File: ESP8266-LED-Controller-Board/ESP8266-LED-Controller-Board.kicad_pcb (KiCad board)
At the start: 2 copper layers, 70 x 38 mm, 52 parts, among them J1 Barrel_Jack_Switch, J2 USB_C_Receptacle_USB2.0, J3 Conn_01x04_Male, J4 Conn_01x05_Male, J5 Screw_Terminal_01x04, J6 Screw_Terminal_01x02, Q1 NTD5867NLT4G, Q2 NTD5867NLT4G, Q3 NTD5867NLT4G, Q4 NTD5867NLT4G, Q5 NTD5867NLT4G, SW1 SW_Push, SW2 SW_Push, U1 TPS563200, U2 ACS70331EESATR-005U3, U3 ESP-12F, U4 74LVC2G17DBVR

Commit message: Updated readme and part number.
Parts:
- U4: value 74LVC2G17DBVR -> SN74LVC2G17DCKR
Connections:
- J2 pad A6: (no net) -> Net-(J2-PadA6)
- J2 pad A7: (no net) -> Net-(J2-PadA7)
- J2 pad A8: (no net) -> Net-(J2-PadA8)
- J2 pad B6: (no net) -> Net-(J2-PadB6)
- J2 pad B7: (no net) -> Net-(J2-PadB7)
- J2 pad B8: (no net) -> Net-(J2-PadB8)
- U3 pad 10: (no net) -> Net-(U3-Pad10)
- U3 pad 13: (no net) -> Net-(U3-Pad13)
- U3 pad 14: (no net) -> Net-(U3-Pad14)
- U3 pad 9: (no net) -> Net-(U3-Pad9)
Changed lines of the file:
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@@
     (zones 0)
     (modules 52)
-    (nets 42)
+    (nets 52)
   )
   (page A4)
@@
   (net 40 "Net-(R7-Pad1)")
   (net 41 "Net-(R11-Pad2)")
+  (net 42 "Net-(J2-PadB6)")
+  (net 43 "Net-(J2-PadA8)")
+  (net 44 "Net-(J2-PadB8)")
+  (net 45 "Net-(J2-PadA7)")
+  (net 46 "Net-(J2-PadA6)")
+  (net 47 "Net-(J2-PadB7)")
+  (net 48 "Net-(U3-Pad14)")
+  (net 49 "Net-(U3-Pad13)")
+  (net 50 "Net-(U3-Pad10)")
+  (net 51 "Net-(U3-Pad9)")
   (net_class Default "This is the default net class."
     (clearance 0.2)
@@
     (add_net "Net-(C2-Pad2)")
     (add_net "Net-(J2-PadA5)")
+    (add_net "Net-(J2-PadA6)")
+    (add_net "Net-(J2-PadA7)")
+    (add_net "Net-(J2-PadA8)")
     (add_net "Net-(J2-PadB5)")
+    (add_net "Net-(J2-PadB6)")
+    (add_net "Net-(J2-PadB7)")
+    (add_net "Net-(J2-PadB8)")
     (add_net "Net-(Q1-Pad1)")
     (add_net "Net-(Q2-Pad1)")
@@
     (add_net "Net-(R5-Pad2)")
     (add_net "Net-(R7-Pad1)")
+    (add_net "Net-(U3-Pad10)")
+    (add_net "Net-(U3-Pad13)")
+    (add_net "Net-(U3-Pad14)")
+    (add_net "Net-(U3-Pad9)")
     (add_net VDD)
     (add_net VIN)
@@
     (pad 15 smd rect (at 7.6 10.5) (size 2.5 1) (layers F.Cu F.Paste F.Mask)
       (net 6 GND))
-    (pad 14 smd rect (at 5 12) (size 1 1.8) (layers F.Cu F.Paste F.Mask))
-    (pad 13 smd rect (at 3 12) (size 1 1.8) (layers F.Cu F.Paste F.Mask))
+    (pad 14 smd rect (at 5 12) (size 1 1.8) (layers F.Cu F.Paste F.Mask)
+      (net 48 "Net-(U3-Pad14)"))
+    (pad 13 smd rect (at 3 12) (size 1 1.8) (layers F.Cu F.Paste F.Mask)
+      (net 49 "Net-(U3-Pad13)"))
     (pad 12 smd rect (at 1 12) (size 1 1.8) (layers F.Cu F.Paste F.Mask)
       (net 28 /LED_G_CTRL))
     (pad 11 smd rect (at -1 12) (size 1 1.8) (layers F.Cu F.Paste F.Mask)
       (net 29 /LED_B_CTRL))
-    (pad 10 smd rect (at -3 12) (size 1 1.8) (layers F.Cu F.Paste F.Mask))
-    (pad 9 smd rect (at -5 12) (size 1 1.8) (layers F.Cu F.Paste F.Mask))
+    (pad 10 smd rect (at -3 12) (size 1 1.8) (layers F.Cu F.Paste F.Mask)
+      (net 50 "Net-(U3-Pad10)"))
+    (pad 9 smd rect (at -5 12) (size 1 1.8) (layers F.Cu F.Paste F.Mask)
+      (net 51 "Net-(U3-Pad9)"))
     (pad 8 smd rect (at -7.6 10.5) (size 2.5 1) (layers F.Cu F.Paste F.Mask)
       (net 7 +3V3))
@@
     (pad B5 smd rect (at 1.75 -2.51 90) (size 0.3 1.16) (layers F.Cu F.Paste F.Mask)
       (net 35 "Net-(J2-PadB5)"))
-    (pad B6 smd rect (at 0.75 -2.51 90) (size 0.3 1.16) (layers F.Cu F.Paste F.Mask))
-    (pad A8 smd rect (at 1.25 -2.51 90) (size 0.3 1.16) (layers F.Cu F.Paste F.Mask))
+    (pad B6 smd rect (at 0.75 -2.51 90) (size 0.3 1.16) (layers F.Cu F.Paste F.Mask)
+      (net 42 "Net-(J2-PadB6)"))
+    (pad A8 smd rect (at 1.25 -2.51 90) (size 0.3 1.16) (layers F.Cu F.Paste F.Mask)
+      (net 43 "Net-(J2-PadA8)"))
     (pad A5 smd rect (at -1.25 -2.51 90) (size 0.3 1.16) (layers F.Cu F.Paste F.Mask)
       (net 36 "Net-(J2-PadA5)"))
-    (pad B8 smd rect (at -1.75 -2.51 90) (size 0.3 1.16) (layers F.Cu F.Paste F.Mask))
-    (pad A7 smd rect (at 0.25 -2.51 90) (size 0.3 1.16) (layers F.Cu F.Paste F.Mask))
-    (pad A6 smd rect (at -0.25 -2.51 90) (size 0.3 1.16) (layers F.Cu F.Paste F.Mask))
-    (pad B7 smd rect (at -0.75 -2.51 90) (size 0.3 1.16) (layers F.Cu F.Paste F.Mask))
+    (pad B8 smd rect (at -1.75 -2.51 90) (size 0.3 1.16) (layers F.Cu F.Paste F.Mask)
+      (net 44 "Net-(J2-PadB8)"))
+    (pad A7 smd rect (at 0.25 -2.51 90) (size 0.3 1.16) (layers F.Cu F.Paste F.Mask)
+      (net 45 "Net-(J2-PadA7)"))
+    (pad A6 smd rect (at -0.25 -2.51 90) (size 0.3 1.16) (layers F.Cu F.Paste F.Mask)
+      (net 46 "Net-(J2-PadA6)"))
+    (pad B7 smd rect (at -0.75 -2.51 90) (size 0.3 1.16) (layers F.Cu F.Paste F.Mask)
+      (net 47 "Net-(J2-PadB7)"))
     (pad S1 thru_hole oval (at 4.32 2.24) (size 1.7 0.9) (drill oval 1.4 0.6) (layers *.Cu *.Mask)
       (net 6 GND))
@@
       (effects (font (size 1 1) (thickness 0.15)))
     )
-    (fp_text value 74LVC2G17DBVR (at 0 2.9) (layer F.Fab)
-      (effects (font (size 1 1) (thickness 0.15)))
-    )
+    (fp_text value SN74LVC2G17DCKR (at 0 2.9) (layer F.Fab)
+      (effects (font (size 1 1) (thickness 0.15)))
+    )

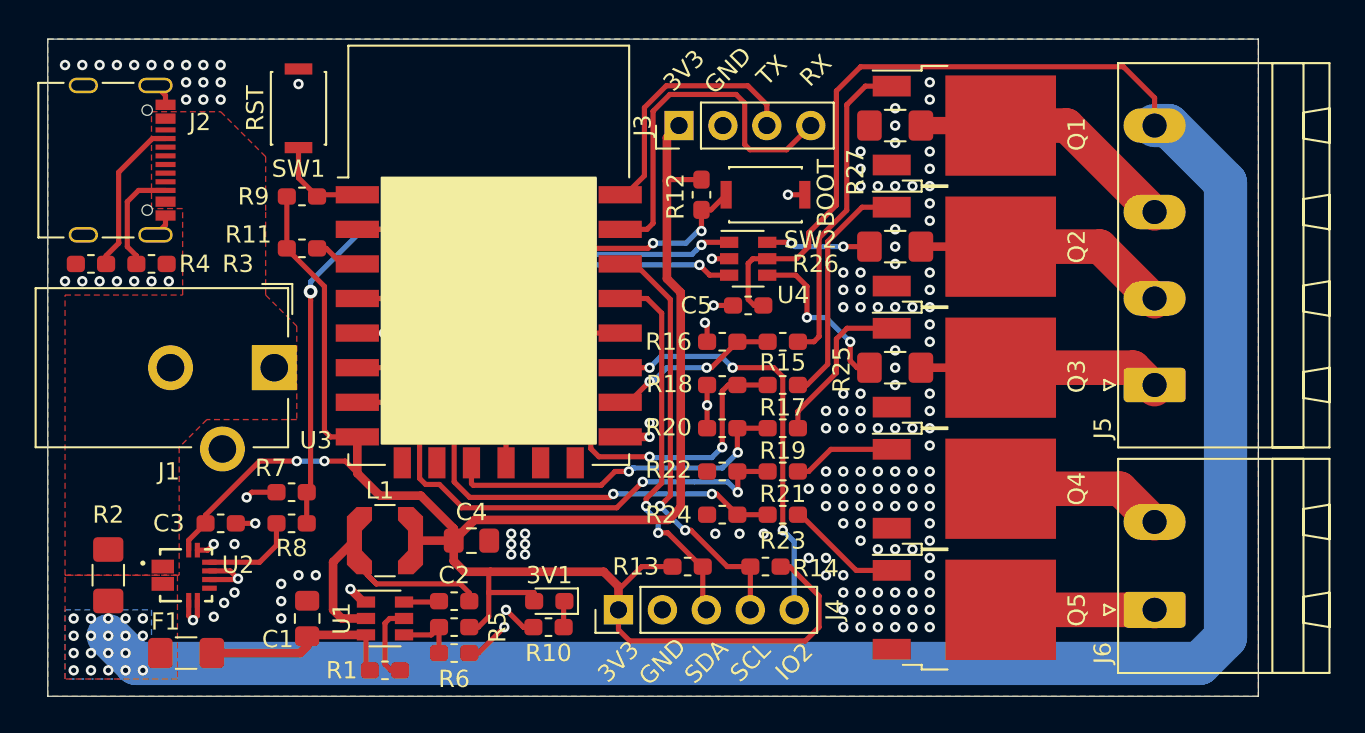
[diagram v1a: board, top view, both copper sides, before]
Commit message: Fixed errors in version 1 of the board.
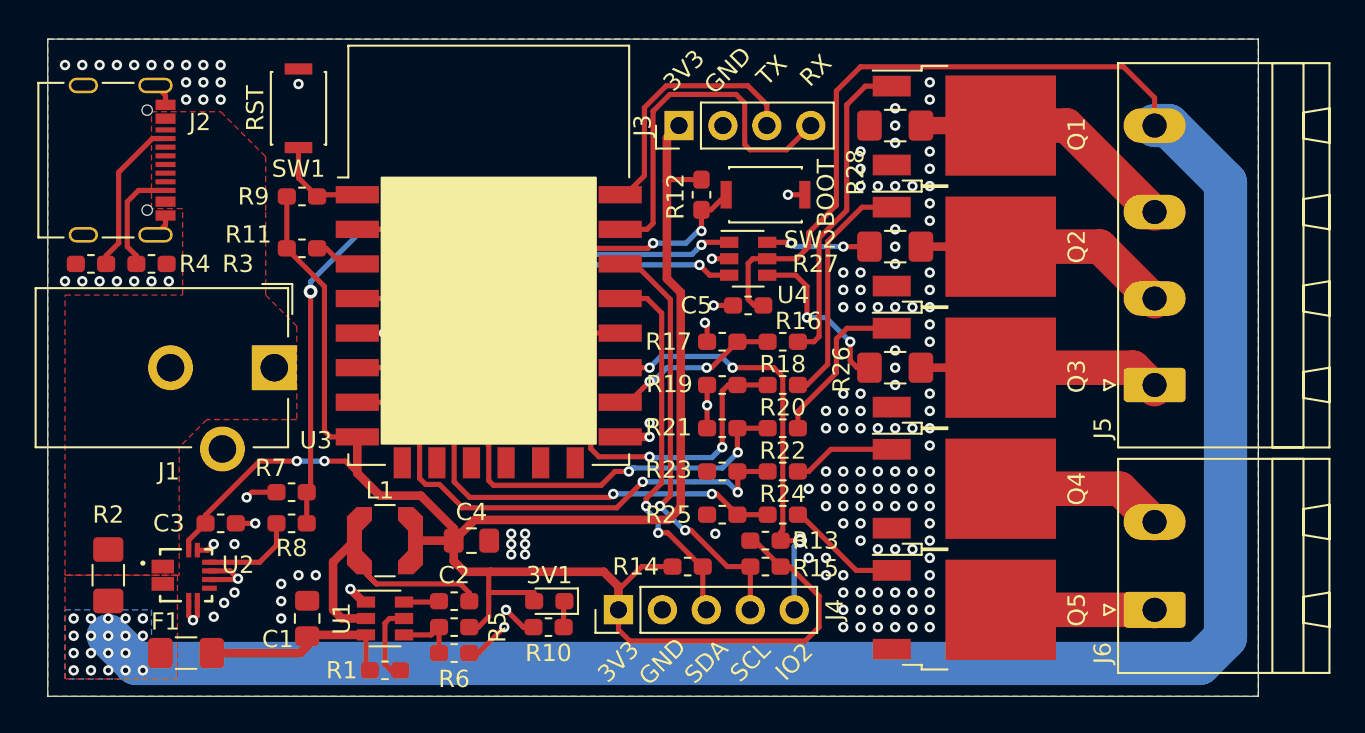
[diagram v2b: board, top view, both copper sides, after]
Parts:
- added R13: 10k, Resistor_SMD:R_0603_1608Metric_Pad1.05x0.95mm_HandSolder, F.Cu at (141.5, 79.0)
- renumbered R13 to R14, R14 to R15, R15 to R16, R16 to R17, R17 to R18, R18 to R19, R19 to R20, R20 to R21, R21 to R22, R22 to R23, R23 to R24, R24 to R25, R25 to R26, R26 to R27, R27 to R28
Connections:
- J2 pad A6: Net-(J2-PadA6) -> (no net)
- J2 pad A7: Net-(J2-PadA7) -> (no net)
- J2 pad A8: Net-(J2-PadA8) -> (no net)
- J2 pad B6: Net-(J2-PadB6) -> (no net)
- J2 pad B7: Net-(J2-PadB7) -> (no net)
- J2 pad B8: Net-(J2-PadB8) -> (no net)
- R18 pad 2: /LED_G_CTRL -> /PIXEL_CLK_3V3-LED_G_CTRL
- R19 pad 2: /LED_G_CTRL -> /PIXEL_CLK_3V3-LED_G_CTRL
- R20 pad 2: /LED_B_CTRL -> /PIXEL_DATA_3V3-LED_B_CTRL
- R21 pad 2: /LED_B_CTRL -> /PIXEL_DATA_3V3-LED_B_CTRL
- U3 pad 10: Net-(U3-Pad10) -> (no net)
- U3 pad 11: /LED_B_CTRL -> (no net)
- U3 pad 12: /LED_G_CTRL -> (no net)
- U3 pad 13: Net-(U3-Pad13) -> (no net)
- U3 pad 14: Net-(U3-Pad14) -> (no net)
- U3 pad 5: /PIXEL_DATA_3V3 -> /PIXEL_DATA_3V3-LED_B_CTRL
- U3 pad 7: /PIXEL_CLK_3V3 -> /PIXEL_CLK_3V3-LED_G_CTRL
- U3 pad 9: Net-(U3-Pad9) -> (no net)
- U4 pad 1: /PIXEL_CLK_3V3 -> /PIXEL_CLK_3V3-LED_G_CTRL
- U4 pad 3: /PIXEL_DATA_3V3 -> /PIXEL_DATA_3V3-LED_B_CTRL
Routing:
- net /PIXEL_DATA_3V3-LED_B_CTRL: track 0.00 -> 53.9 mm, vias 0 -> 6
- net /PIXEL_CLK_3V3-LED_G_CTRL: track 0.00 -> 51.5 mm, vias 0 -> 6
- net /PIXEL_CLK_3V3: track 26.2 -> 0.00 mm, vias 4 -> 0
- net /PIXEL_DATA_3V3: track 25.0 -> 0.00 mm, vias 4 -> 0
- net /LED_G_CTRL: track 21.0 -> 0.00 mm, vias 2 -> 0
- net /LED_B_CTRL: track 20.6 -> 0.00 mm, vias 2 -> 0
- net +3V3: track 122.7 -> 125.1 mm
- net /GPIO2: track 23.9 -> 25.0 mm
- net GND: vias 162 -> 160

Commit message: Fixed wrong footprint.
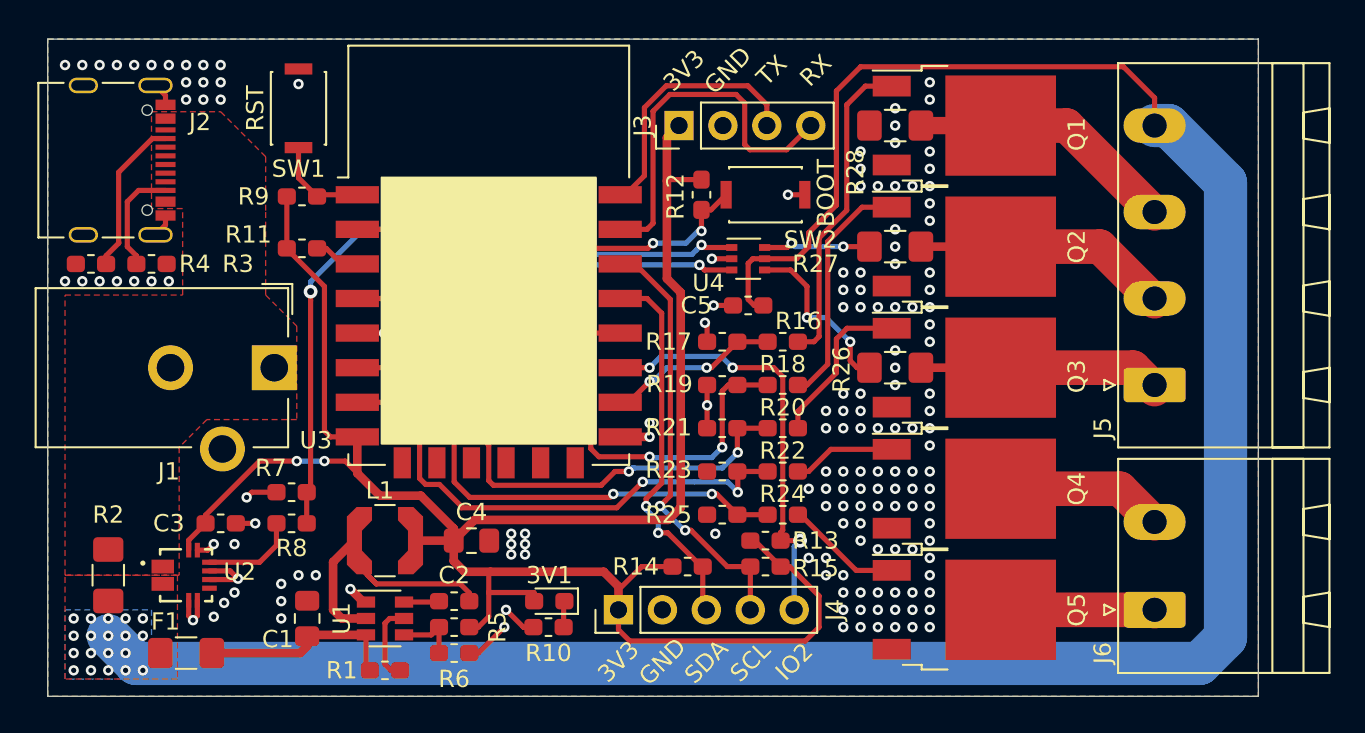
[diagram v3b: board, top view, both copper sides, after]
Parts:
- U4: footprint Package_TO_SOT_SMD:SOT-23-6 -> Package_TO_SOT_SMD:SOT-363_SC-70-6

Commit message: Fixed wrong designator on LED.
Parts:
- renumbered 3V1 to 3V3

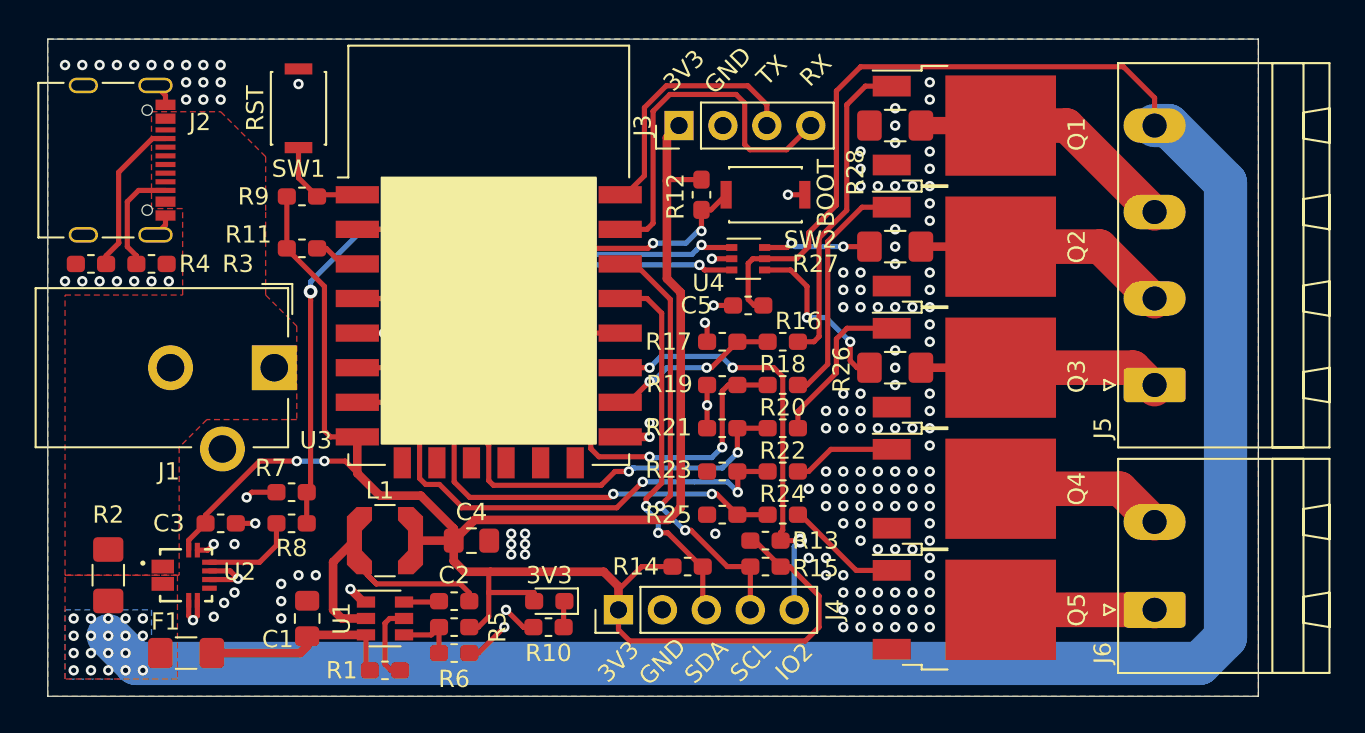
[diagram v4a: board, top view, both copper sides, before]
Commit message: Changed buffers to SN74LV1T34DCKR because the previous SN74LVC2G17DCKR do not work well with 3.3V logic when VCC is 5V. Changed passive footprints to non-handsolder version.
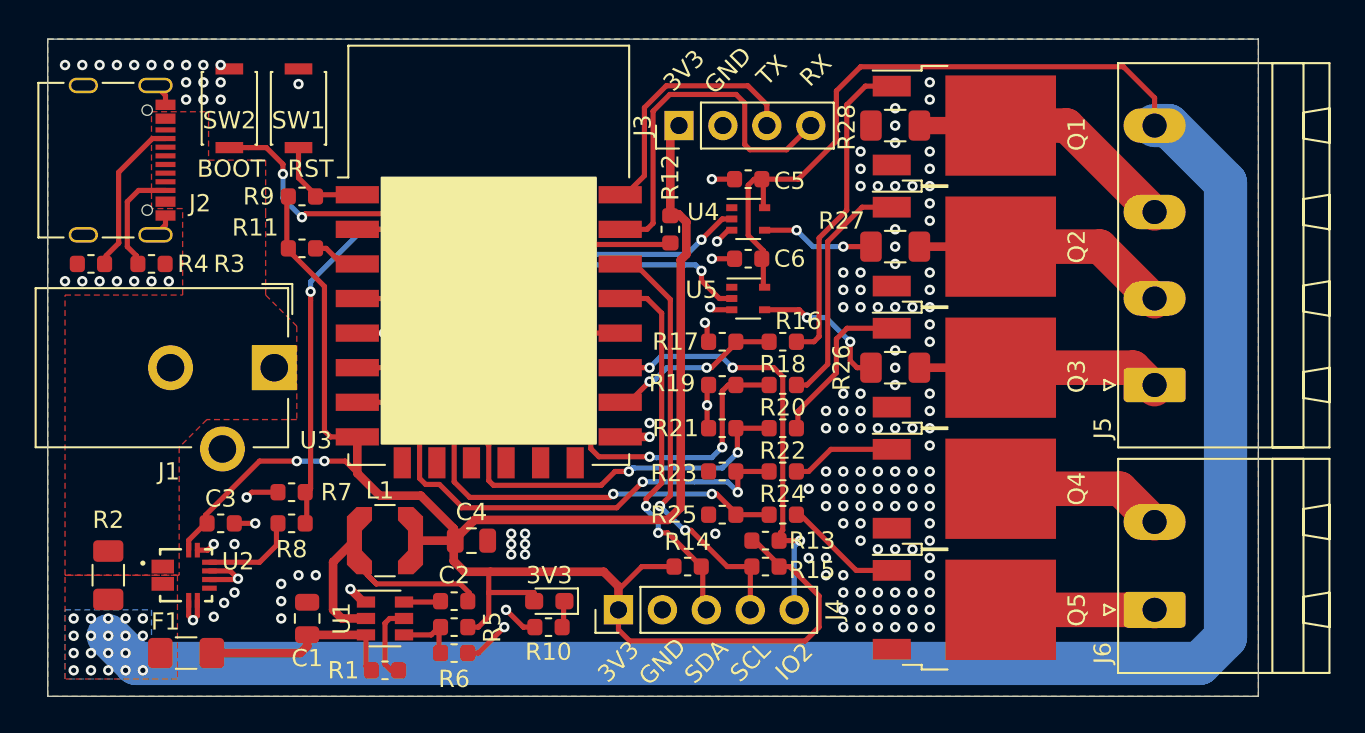
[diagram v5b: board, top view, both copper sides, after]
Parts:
- added C6: 100n, Capacitor_SMD:C_0603_1608Metric, F.Cu at (140.5, 62.7)
- added U5: SN74LV1T34DCKR, Package_TO_SOT_SMD:SOT-353_SC-70-5, F.Cu at (140.5, 65.0)
- C1, C4: footprint Capacitor_SMD:C_0805_2012Metric_Pad1.15x1.40mm_HandSolder -> Capacitor_SMD:C_0805_2012Metric
- C2, C3, C5: footprint Capacitor_SMD:C_0603_1608Metric_Pad1.05x0.95mm_HandSolder -> Capacitor_SMD:C_0603_1608Metric
- R1, R10, R11, R12, R13, R14, R15, R16, R17, R18, R19, R20, R21, R22, R23, R24, R25, R3, R4, R5, R6, R7, R8, R9: footprint Resistor_SMD:R_0603_1608Metric_Pad1.05x0.95mm_HandSolder -> Resistor_SMD:R_0603_1608Metric
- R2, R26, R27, R28: footprint Resistor_SMD:R_1206_3216Metric_Pad1.42x1.75mm_HandSolder -> Resistor_SMD:R_1206_3216Metric
- U4: value SN74LVC2G17DCKR -> SN74LV1T34DCKR; footprint Package_TO_SOT_SMD:SOT-363_SC-70-6 -> Package_TO_SOT_SMD:SOT-353_SC-70-5
- moved SW2 31.4 mm to (110.5, 54.0), turned to 90 degrees
- moved C5 7.30 mm to (140.5, 58.1)
- moved R12 2.69 mm to (136.0, 61.0)
- moved U4 2.30 mm to (140.5, 60.4)
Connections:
- R18 pad 2: /PIXEL_CLK_3V3-LED_G_CTRL -> /PIXEL_DATA_3V3-LED_G_CTRL
- R19 pad 2: /PIXEL_CLK_3V3-LED_G_CTRL -> /PIXEL_DATA_3V3-LED_G_CTRL
- R20 pad 2: /PIXEL_DATA_3V3-LED_B_CTRL -> /PIXEL_CLK_3V3-LED_B_CTRL
- R21 pad 2: /PIXEL_DATA_3V3-LED_B_CTRL -> /PIXEL_CLK_3V3-LED_B_CTRL
- R26 pad 1: /PIXEL_DATA_5V -> /PIXEL_CLK_5V
- R27 pad 1: /PIXEL_CLK_5V -> /PIXEL_DATA_5V
- U3 pad 5: /PIXEL_DATA_3V3-LED_B_CTRL -> /PIXEL_CLK_3V3-LED_B_CTRL
- U3 pad 7: /PIXEL_CLK_3V3-LED_G_CTRL -> /PIXEL_DATA_3V3-LED_G_CTRL
- U4 pad 1: /PIXEL_CLK_3V3-LED_G_CTRL -> (no net)
- U4 pad 2: GND -> /PIXEL_DATA_3V3-LED_G_CTRL
- U4 pad 3: /PIXEL_DATA_3V3-LED_B_CTRL -> GND
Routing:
- net /PIXEL_CLK_3V3-LED_B_CTRL: track 0.00 -> 54.9 mm, vias 0 -> 6
- net /PIXEL_DATA_3V3-LED_B_CTRL: track 53.9 -> 0.00 mm, vias 6 -> 0
- net /PIXEL_DATA_3V3-LED_G_CTRL: track 0.00 -> 52.2 mm, vias 0 -> 6
- net /PIXEL_CLK_3V3-LED_G_CTRL: track 51.6 -> 0.00 mm, vias 6 -> 0
- net /BOOT: track 16.3 -> 36.1 mm
- net /PIXEL_DATA_5V: track 10.1 -> 6.46 mm
- net /PIXEL_CLK_5V: track 6.25 -> 8.09 mm
- net GND: track 27.1 -> 28.9 mm, vias 160 -> 161
- net +3V3: track 125.1 -> 123.4 mm
